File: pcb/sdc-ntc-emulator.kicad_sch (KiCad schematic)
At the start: 55 parts, among them J1 DevKit J1, J2 DevKit J3, J3 5V IN (RAC03), J4 SDC VE1 / GND, J5 SDC SERVICE, J6 EXT I/O, J7 USB-C 5V IN, K1 G5V-2-H1 5VDC, Q1 AO3400A, Q2 AO3401A, U1 ISO1540, U2 AD5272BRMZ-50, U3 ISO7721D

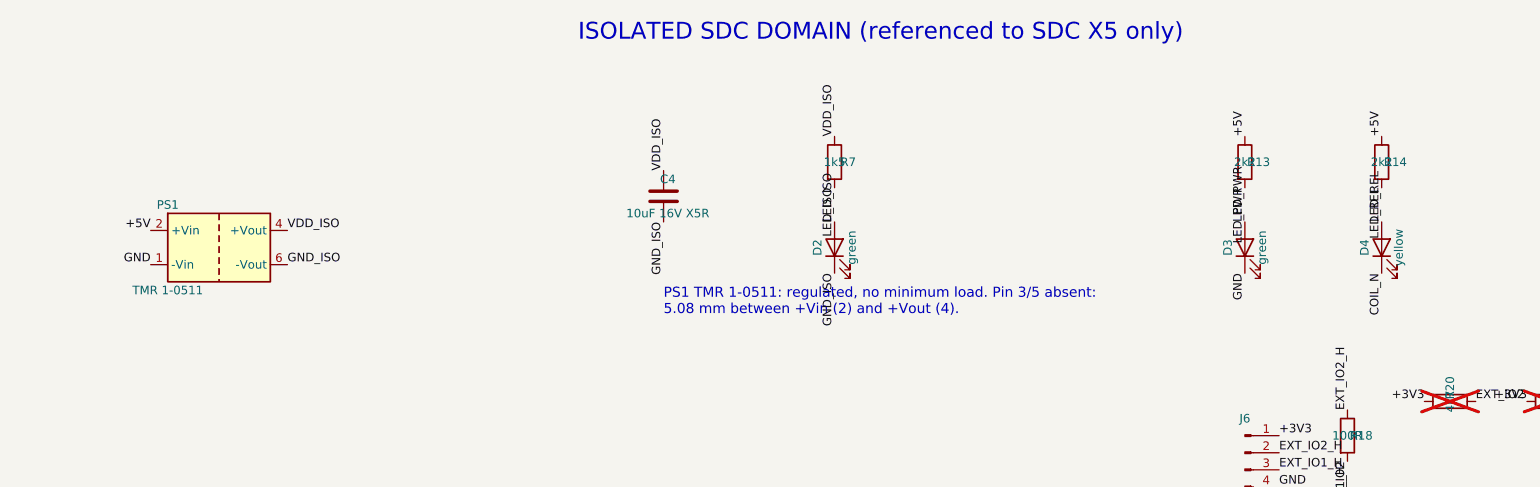
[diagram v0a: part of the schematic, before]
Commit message: PCB rev 4; restructure for public release
PCB rev 4: Gaptec 1S4E_0509S1U + L78L05 replace the TMR 1-0511 as the
isolated supply (isolation gap 1.14 mm, ERC/DRC clean).

Repository layout for publication:
- hardware/sdc-ntc-emulator/ -> pcb/, handoff -> docs/design-notes.md
- firmware/ with pin map and plan (firmware not written yet)
- top-level README, CERN-OHL-S-2.0 (hardware, docs) and
  GPL-3.0-or-later (pcb/tools, firmware)
- build scripts take KiCad paths from environment variables
- schematic PDF published; datasheets and local files git-ignored

Co-Authored-By: Claude Opus 5.5 <noreply@anthropic.com>
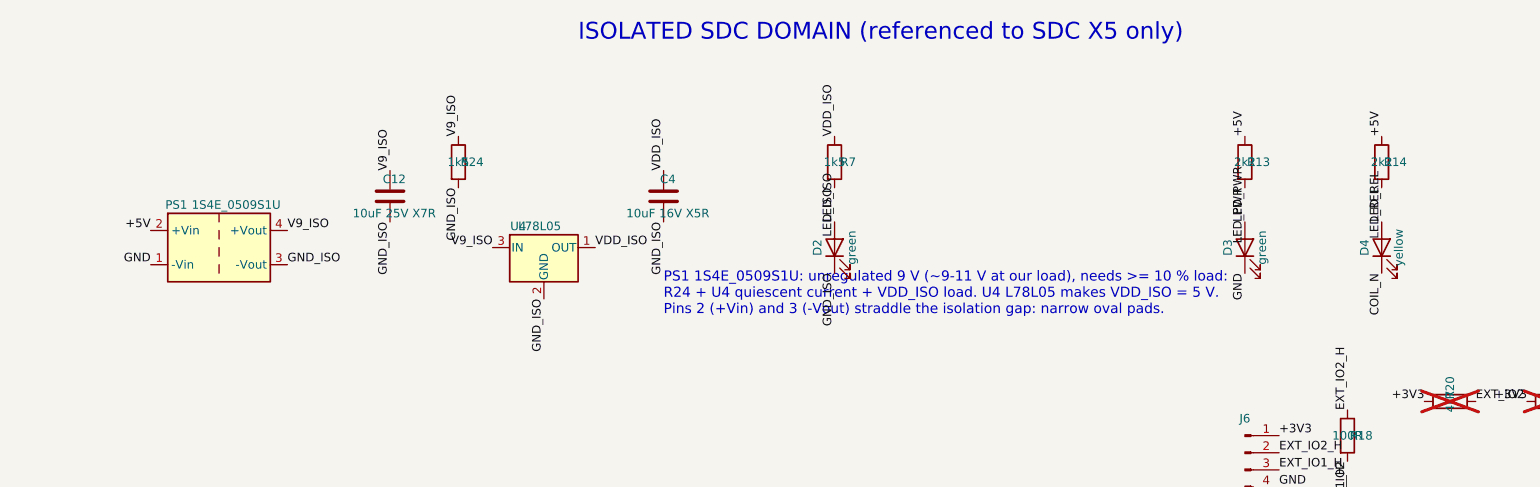
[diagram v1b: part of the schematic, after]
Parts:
- added C12: 10uF 25V X7R, Capacitor_SMD:C_1206_3216Metric_Pad1.33x1.80mm_HandSolder, symbol Device:C
- added R24: 1k5, Resistor_SMD:R_0805_2012Metric_Pad1.20x1.40mm_HandSolder, symbol Device:R
- added U4: L78L05, Package_TO_SOT_SMD:SOT-89-3, symbol Regulator_Linear:L78L05_SOT89
- PS1: value TMR 1-0511 -> 1S4E_0509S1U; footprint Converter_DCDC:Converter_DCDC_TRACO_TMR-1-xxxx_Single_THT -> Converter_DCDC:Converter_DCDC_TRACO_TME_03xxS_05xxS_12xxS_Single_THT; symbol sdc_emulator:TMR1-0511 -> Converter_DCDC:TME-0509S; MPN TMR 1-0511 -> 1S4E_0509S1U; Manufacturer Traco Power -> GAPTEC Electronic
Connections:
- net GND_ISO: now also PS1.3 (-Vout), C12.2, R24.2, U4.2 (GND); no longer PS1.6 (-Vout)
- net VDD_ISO: now also U4.1 (OUT); no longer PS1.4 (+Vout)
- new net V9_ISO: C12.1, PS1.4 (+Vout), R24.1, U4.3 (IN)
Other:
- note added: "PS1 1S4E_0509S1U: unregulated 9 V (~9-11 V at our load), needs >= 10 % load: R24 + U4 quiescent current + VDD_ISO load. U4 L78L05 makes VDD_ISO = 5 V. Pins 2 (+Vin) and 3 (-Vout) straddle the isolation gap: narrow oval pads."
- note removed: "PS1 TMR 1-0511: regulated, no minimum load. Pin 3/5 absent: 5.08 mm between +Vin (2) and +Vout (4)."
